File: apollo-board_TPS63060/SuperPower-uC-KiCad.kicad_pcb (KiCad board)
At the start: 4 copper layers, 45.1 x 45.1 mm, 125 parts, among them J1 JST_PH_S2B_thru, J10 Conn_01x13_Male, J11 Conn_01x04_Male, J2 Barrel_Jack_Switch, J3 Conn_01x02_Male, J4 DNP/JST_ZH_S2B_thru, J5 DNP/JST_XH_S2B_thru, J6 Conn_01x02_Male, Q1 DMN2019UTS, Q10 2N7002A, Q11 2N7002A, Q12 DMP2035UVT, Q13 DMP2035UVT, Q14 DMP2035UVT, Q15 DMN3023L, Q2 Si3421DV, Q3 DMN3023L, Q4 2N7002A, Q5 DMP2035UVT, Q6 BSS84-7-F, Q9 2N7002A, SW1 DNP/SKRKAEE020, U1 AP9101CK6-AYTRG1, U10 TPS63070RNMT, U2 USB-C, U3 IP4220CZ6, U4 LTC4162EUFD-LAD, U5 RV-3028-C7, U8 TPS70933DRVT, U9 TPS63060

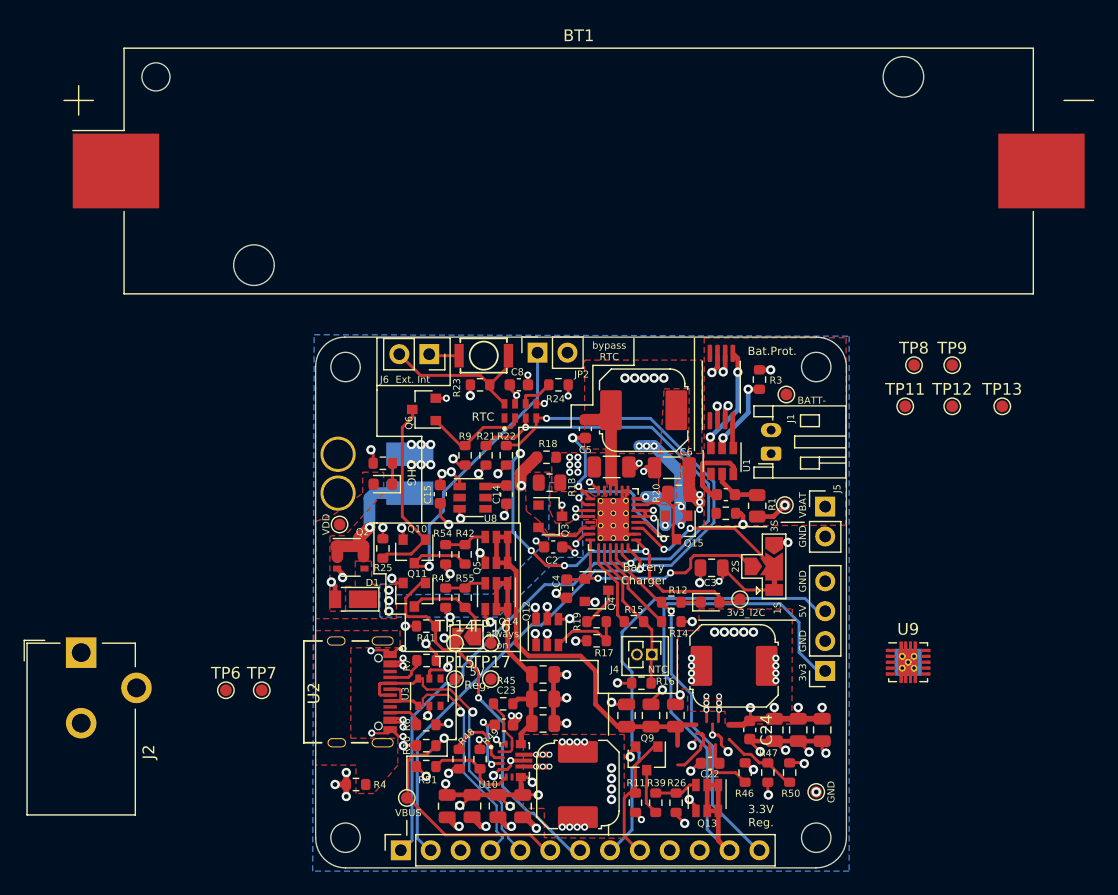
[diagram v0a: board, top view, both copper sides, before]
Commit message: Remove unused parts at schematic level.
+ solve schematic DRC issues
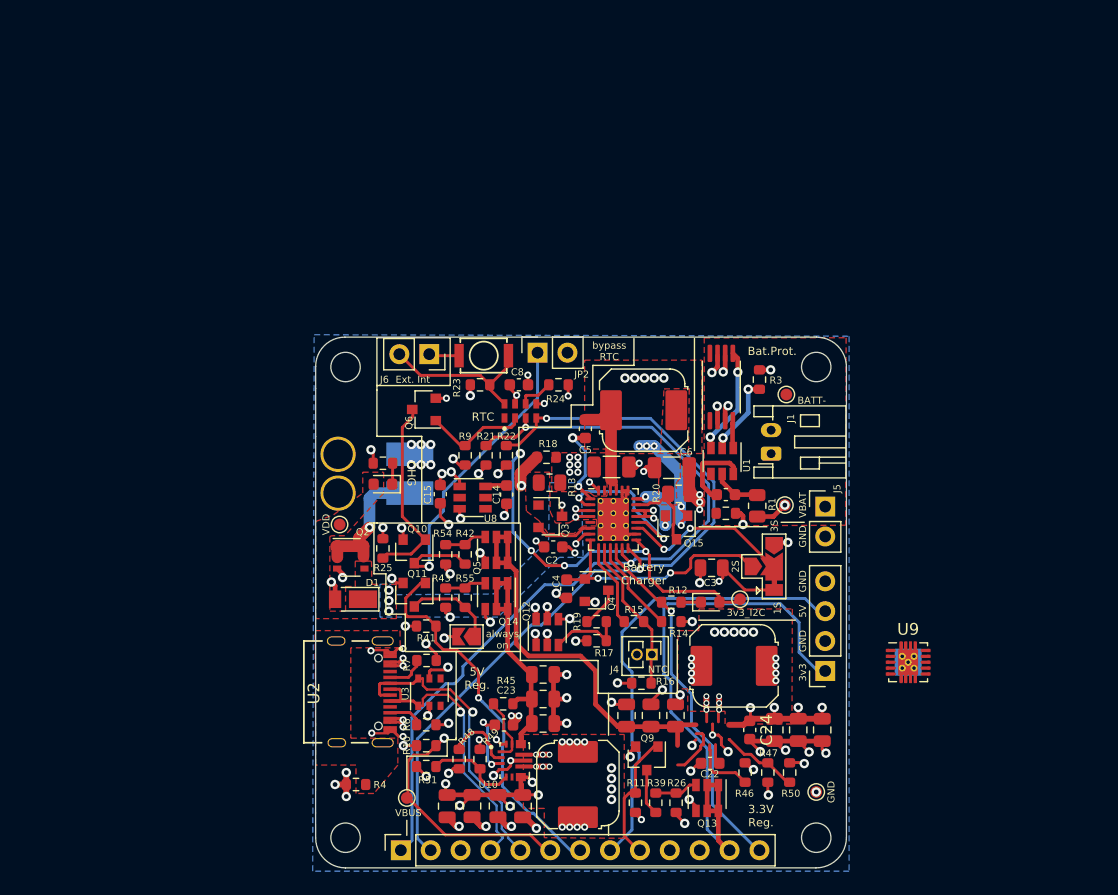
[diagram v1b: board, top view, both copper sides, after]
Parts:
- removed BT1: Battery_Cell_Holder_18650_SMT_1042, Battery:BatteryHolder_Keystone_1042_1x18650
- removed J2: Barrel_Jack_Switch, Connector_BarrelJack:BarrelJack_CUI_PJ-102AH_Horizontal
- removed TP11: SCL, TestPoint:TestPoint_Pad_D1.0mm
- removed TP12: SDA, TestPoint:TestPoint_Pad_D1.0mm
- removed TP13: ~SMBALERT, TestPoint:TestPoint_Pad_D1.0mm
- removed TP14, TP15, TP16, TP17, TP6, TP7: TestPoint, TestPoint:TestPoint_Pad_D1.0mm
- removed TP8: CHARGER_VIN, TestPoint:TestPoint_Pad_D1.0mm
- removed TP9: VOUT, TestPoint:TestPoint_Pad_D1.0mm

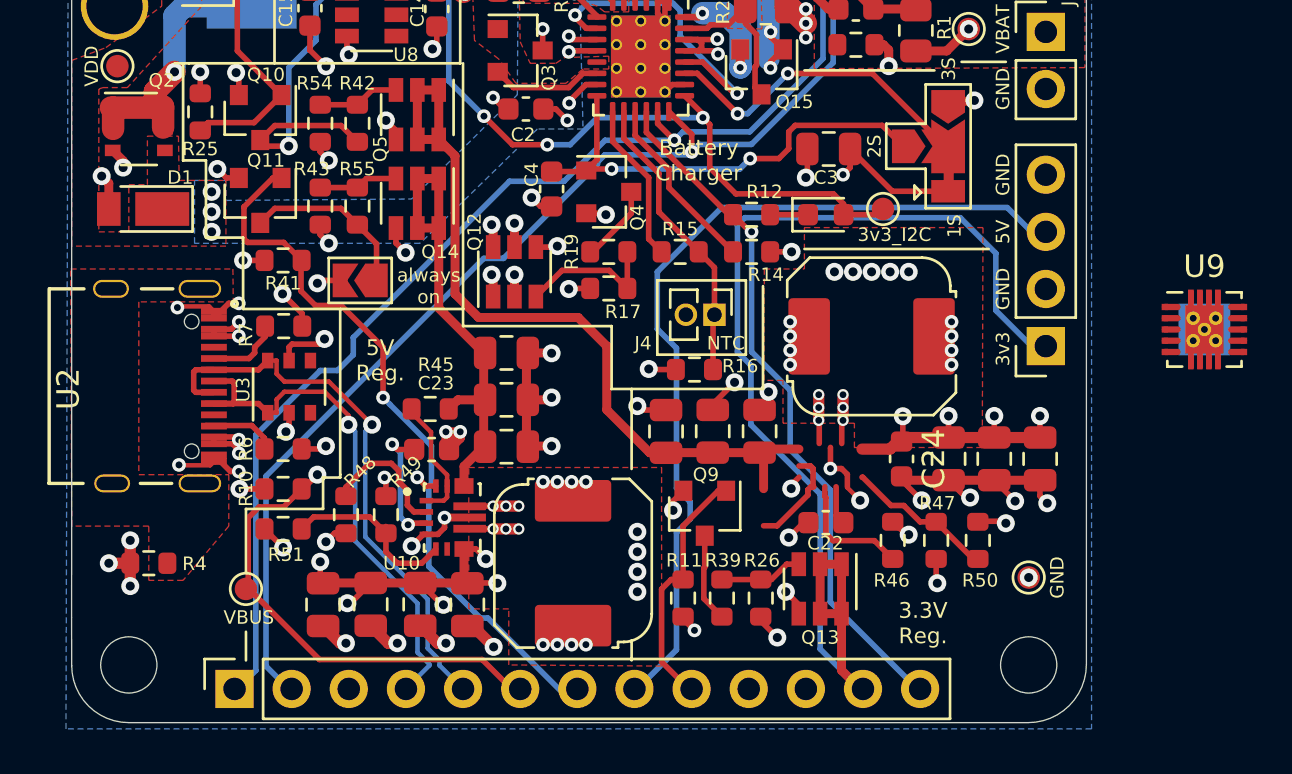
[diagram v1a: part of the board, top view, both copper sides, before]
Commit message: Place and route U9 (TPS63060)
+ re-place other parts
+ re-design planes shapes
+ display some silkscreen Ref. Des
+ misc. improvements.
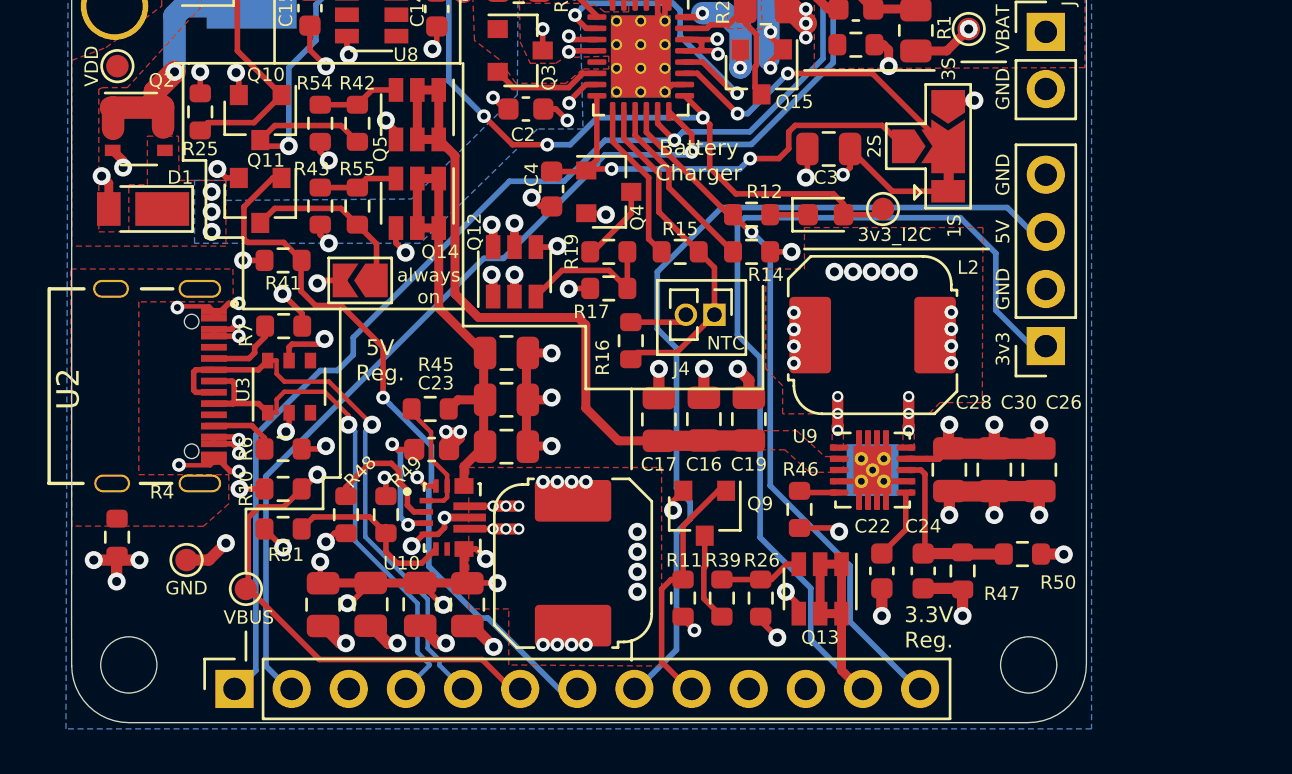
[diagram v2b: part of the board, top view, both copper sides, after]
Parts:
- moved TP3 37.4 mm to (123.1, 113.0)
- moved U9 16.0 mm to (153.6, 109.0)
- moved C24 5.07 mm to (155.8, 113.5)
- moved R46 4.37 mm to (150.3, 110.8), turned to 270 degrees
- moved C22 3.29 mm to (154.0, 113.5), turned to 270 degrees
- moved R16 3.11 mm to (142.8, 103.3), turned to 270 degrees
- moved R50 2.07 mm to (160.2, 112.8), turned to 0 degrees
- moved R4 1.83 mm to (120.0, 112.0), turned to 270 degrees
- moved R47 1.80 mm to (157.6, 113.5)
- moved C19 0.72 mm to (148.1, 106.8)
- moved C16 0.67 mm to (146.1, 106.8)
- moved C17 0.62 mm to (144.1, 106.8)
- moved C28 0.48 mm to (157.0, 109.0)
- moved C30 0.48 mm to (159.0, 109.0)
- moved C26 0.48 mm to (161.0, 109.0)
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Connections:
- net Net-(C16-Pad1) renamed /Regulator and Cut-Off Module/3v3_Reg_Vin
- net Net-(C22-Pad1) renamed /Regulator and Cut-Off Module/3v3_Reg_Vaux
- net Net-(C24-Pad1) renamed /Regulator and Cut-Off Module/3v3_Reg_FB
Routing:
- net GND: track 95.6 -> 103.8 mm, vias 85 -> 80
- net Net-(R44-Pad1): track 4.57 -> 0.00 mm
- net Net-(R46-Pad1): track 5.53 -> 1.60 mm
- net /Regulator and Cut-Off Module/3v3_Reg_Vin: track 35.1 -> 31.4 mm
- net Net-(L2-Pad2): track 4.16 -> 1.52 mm
- net Net-(L2-Pad1): track 3.71 -> 1.50 mm
- net /Charging Module/NTC: track 13.2 -> 15.3 mm
- net /3v3_MCU: track 16.6 -> 14.5 mm, vias 8 -> 7
- net /Regulator and Cut-Off Module/3v3_Reg_FB: track 6.66 -> 8.34 mm
- net /Regulator and Cut-Off Module/3v3_Reg_Vaux: track 1.73 -> 3.15 mm
- added copper zone on F.Cu, net /Regulator and Cut-Off Module/3v3_Reg_Vin
- added copper zone on F.Cu, net Net-(L2-Pad1)
- added copper zone on F.Cu, net Net-(L2-Pad2)

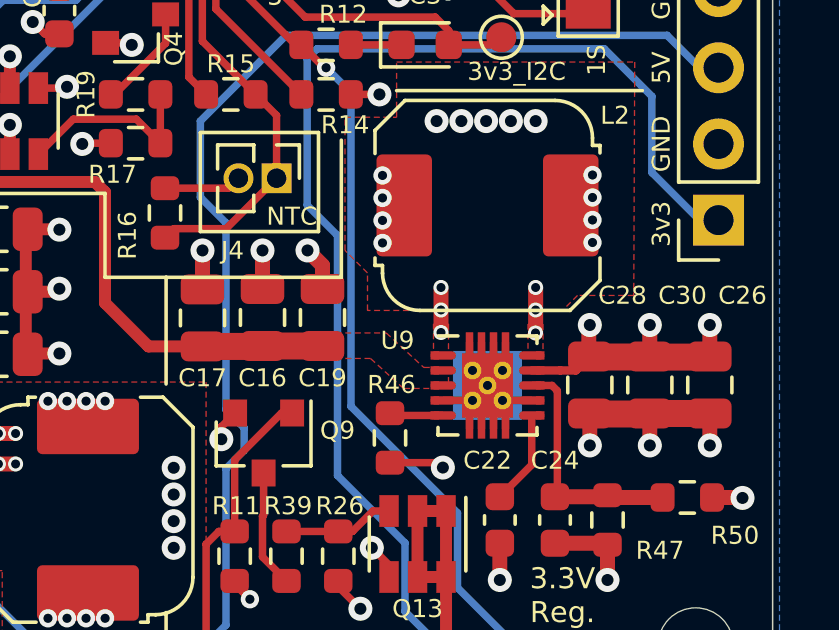
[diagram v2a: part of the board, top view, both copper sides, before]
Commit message: Add TPS63060 component files
+ 3D package
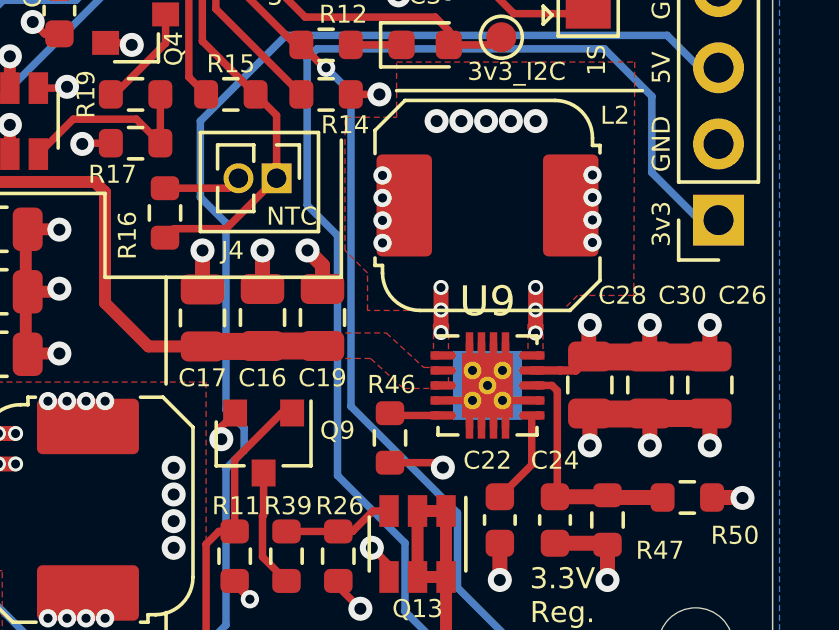
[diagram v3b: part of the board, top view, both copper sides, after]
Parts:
- U9: footprint Package_SON:Texas_S-PWSON-N10_ThermalVias -> TPS63060:Texas_S-PWSON-N10_ThermalVias

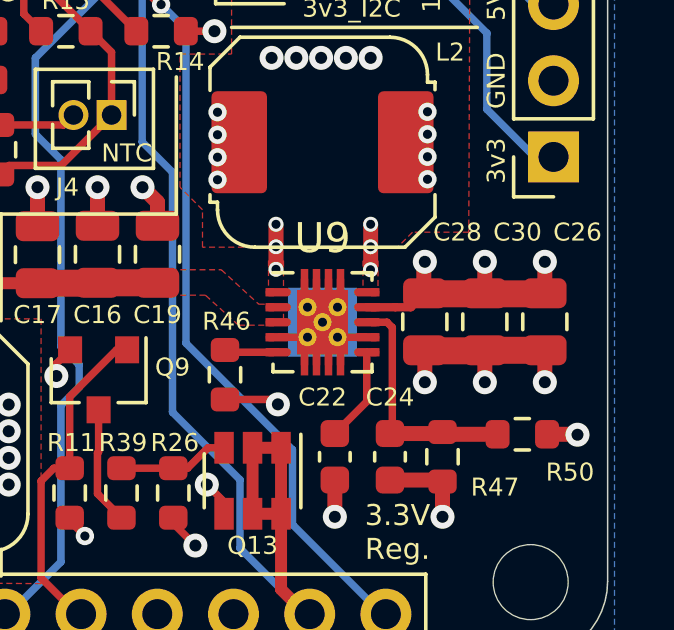
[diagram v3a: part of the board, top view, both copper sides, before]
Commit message: Update 22µF 0805 & 100nF 0603 capacitors
around TPS63060
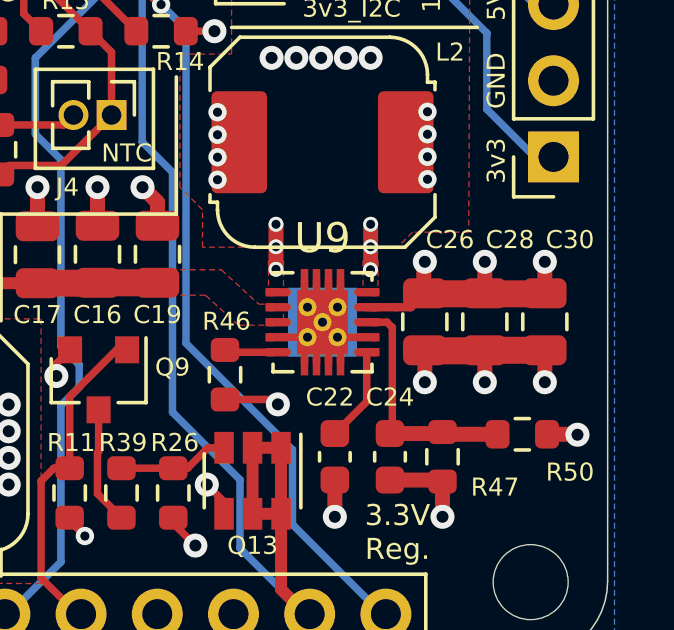
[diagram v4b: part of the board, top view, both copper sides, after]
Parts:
- C22: value 0.1µF -> CL10B104KB8NNNC
- C26, C28, C30: value 22μF -> CL21A226MAQNNNE
- moved C26 4.00 mm to (157.0, 109.0)
- moved C28 2.00 mm to (159.0, 109.0)
- moved C30 2.00 mm to (161.0, 109.0)

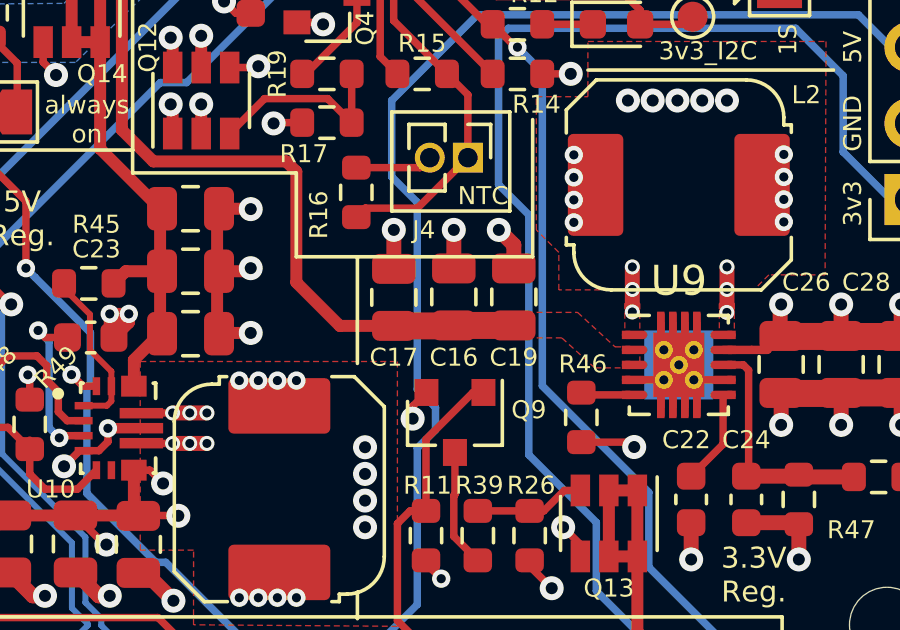
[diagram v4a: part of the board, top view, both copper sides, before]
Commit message: Update 10µF 0805 capacitors
Around TPS63060
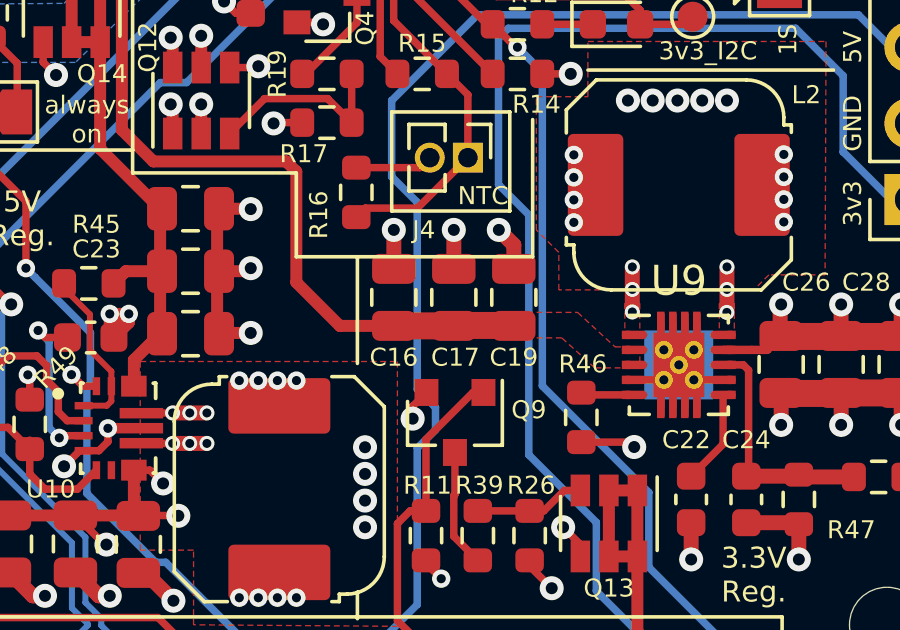
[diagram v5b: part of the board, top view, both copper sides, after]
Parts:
- C16, C17, C19: value 10μF -> CL21A106KAYNNNE
- moved C16 2.00 mm to (144.1, 106.8)
- moved C17 2.00 mm to (146.1, 106.8)

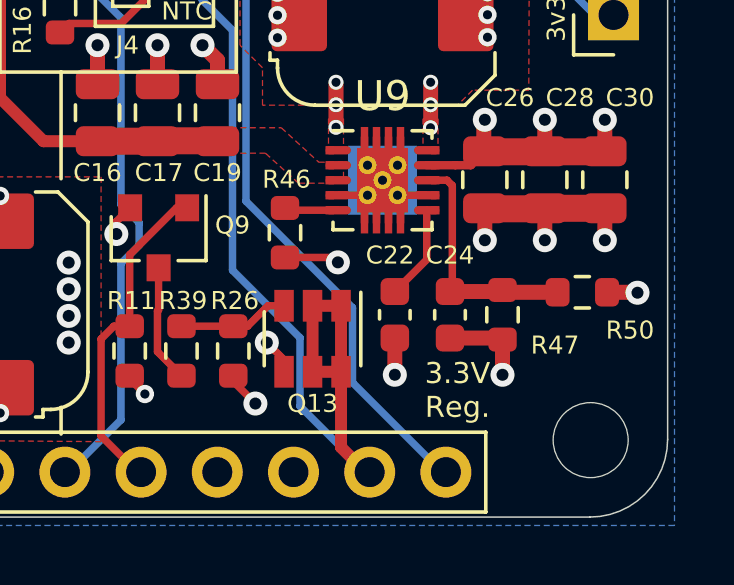
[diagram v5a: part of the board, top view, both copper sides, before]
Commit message: Update 10pF 0603 capacitor
around TPS63060
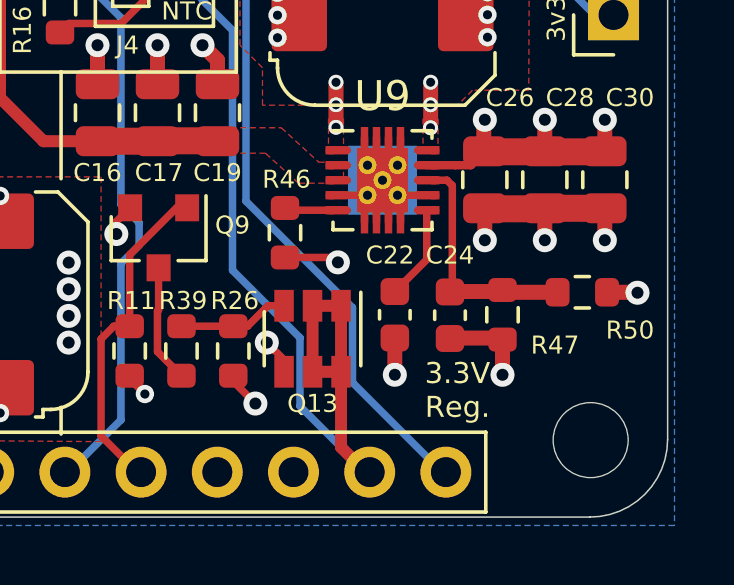
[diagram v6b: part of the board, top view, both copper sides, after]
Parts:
- C24: value 10pF -> CC0603JRNPO9BN100
